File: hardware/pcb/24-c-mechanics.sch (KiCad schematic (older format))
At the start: 24 parts, among them U301 VID28-05, U302 VID66-08, U303 AH3572, U304 AH3572, U305 AH3572, U306 AH3572

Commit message: First placement
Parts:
- removed TP301: MA1, TestPoint:TestPoint_Pad_D2.0mm, symbol Connector:TestPoint
- removed TP302: MA2, TestPoint:TestPoint_Pad_D2.0mm, symbol Connector:TestPoint
- removed TP304: MA3, TestPoint:TestPoint_Pad_D2.0mm, symbol Connector:TestPoint
- removed TP307: MA4, TestPoint:TestPoint_Pad_D2.0mm, symbol Connector:TestPoint
- removed TP310: MB1, TestPoint:TestPoint_Pad_D2.0mm, symbol Connector:TestPoint
- removed TP311: MB2, TestPoint:TestPoint_Pad_D2.0mm, symbol Connector:TestPoint
- removed TP312: MB3, TestPoint:TestPoint_Pad_D2.0mm, symbol Connector:TestPoint
- removed TP313: MB4, TestPoint:TestPoint_Pad_D2.0mm, symbol Connector:TestPoint
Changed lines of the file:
@@
 	6750 4300 7500 4300
-$Comp
-L Connector:TestPoint TP301
-U 1 1 5FF9F67F
-P 9350 1500
-F 0 "TP301" V 9350 1700 50  0000 L CNN
-F 1 "MA1" H 9408 1527 50  0001 L CNN
-F 2 "TestPoint:TestPoint_Pad_D2.0mm" H 9550 1500 50  0001 C CNN
-F 3 "~" H 9550 1500 50  0001 C CNN
-	1    9350 1500
-	0    1    -1   0
-$EndComp
-$Comp
-L Connector:TestPoint TP302
-U 1 1 5FFA0591
-P 9350 1600
-F 0 "TP302" V 9350 1800 50  0000 L CNN
-F 1 "MA2" H 9408 1627 50  0001 L CNN
-F 2 "TestPoint:TestPoint_Pad_D2.0mm" H 9550 1600 50  0001 C CNN
-F 3 "~" H 9550 1600 50  0001 C CNN
-	1    9350 1600
-	0    1    -1   0
-$EndComp
-$Comp
-L Connector:TestPoint TP304
-U 1 1 5FFA0852
-P 9350 1700
-F 0 "TP304" V 9350 1900 50  0000 L CNN
-F 1 "MA3" H 9408 1727 50  0001 L CNN
-F 2 "TestPoint:TestPoint_Pad_D2.0mm" H 9550 1700 50  0001 C CNN
-F 3 "~" H 9550 1700 50  0001 C CNN
-	1    9350 1700
-	0    1    -1   0
-$EndComp
-$Comp
-L Connector:TestPoint TP307
-U 1 1 5FFA0AC7
-P 9350 1800
-F 0 "TP307" V 9350 2000 50  0000 L CNN
-F 1 "MA4" H 9408 1827 50  0001 L CNN
-F 2 "TestPoint:TestPoint_Pad_D2.0mm" H 9550 1800 50  0001 C CNN
-F 3 "~" H 9550 1800 50  0001 C CNN
-	1    9350 1800
-	0    1    -1   0
-$EndComp
-Wire Wire Line
-	9350 1500 8950 1500
-Wire Wire Line
-	9350 1600 8950 1600
-Wire Wire Line
-	9350 1700 8950 1700
-Wire Wire Line
-	9350 1800 8950 1800
-$Comp
-L Connector:TestPoint TP310
-U 1 1 5FFAB35D
-P 9350 2250
-F 0 "TP310" V 9350 2450 50  0000 L CNN
-F 1 "MB1" H 9408 2277 50  0001 L CNN
-F 2 "TestPoint:TestPoint_Pad_D2.0mm" H 9550 2250 50  0001 C CNN
-F 3 "~" H 9550 2250 50  0001 C CNN
-	1    9350 2250
-	0    1    -1   0
-$EndComp
-$Comp
-L Connector:TestPoint TP311
-U 1 1 5FFAB363
-P 9350 2350
-F 0 "TP311" V 9350 2550 50  0000 L CNN
-F 1 "MB2" H 9408 2377 50  0001 L CNN
-F 2 "TestPoint:TestPoint_Pad_D2.0mm" H 9550 2350 50  0001 C CNN
-F 3 "~" H 9550 2350 50  0001 C CNN
-	1    9350 2350
-	0    1    -1   0
-$EndComp
-$Comp
-L Connector:TestPoint TP312
-U 1 1 5FFAB369
-P 9350 2450
-F 0 "TP312" V 9350 2650 50  0000 L CNN
-F 1 "MB3" H 9408 2477 50  0001 L CNN
-F 2 "TestPoint:TestPoint_Pad_D2.0mm" H 9550 2450 50  0001 C CNN
-F 3 "~" H 9550 2450 50  0001 C CNN
-	1    9350 2450
-	0    1    -1   0
-$EndComp
-$Comp
-L Connector:TestPoint TP313
-U 1 1 5FFAB36F
-P 9350 2550
-F 0 "TP313" V 9350 2750 50  0000 L CNN
-F 1 "MB4" H 9408 2577 50  0001 L CNN
-F 2 "TestPoint:TestPoint_Pad_D2.0mm" H 9550 2550 50  0001 C CNN
-F 3 "~" H 9550 2550 50  0001 C CNN
-	1    9350 2550
-	0    1    -1   0
-$EndComp
-Wire Wire Line
-	9350 2250 8950 2250
-Wire Wire Line
-	9350 2350 8950 2350
-Wire Wire Line
-	9350 2450 8950 2450
-Wire Wire Line
-	9350 2550 8950 2550
-Text Label 8950 1500 0    50   ~ 0
-MA1
-Text Label 8950 1600 0    50   ~ 0
-MA2
-Text Label 8950 1700 0    50   ~ 0
-MA3
-Text Label 8950 1800 0    50   ~ 0
-MA4
-Text Label 8950 2250 0    50   ~ 0
-MB1
-Text Label 8950 2350 0    50   ~ 0
-MB2
-Text Label 8950 2450 0    50   ~ 0
-MB3
-Text Label 8950 2550 0    50   ~ 0
-MB4
 $Comp
 L Connector:TestPoint TP309

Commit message: Finished routing
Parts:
- U301: footprint mvl-footprints:vid_28_05 -> mvl-footprints:BK30D-R5
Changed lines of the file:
@@
 F 0 "U301" H 8050 1865 50  0000 C CNN
 F 1 "VID28-05" H 8050 1774 50  0000 C CNN
-F 2 "mvl-footprints:vid_28_05" H 8050 1150 50  0001 C CNN
+F 2 "mvl-footprints:BK30D-R5" H 8050 1150 50  0001 C CNN
 F 3 "http://www.vidmotion.com.cn/UploadFile/pdf/product/20090905105654VID28-05%20V2070829.pdf" H 7700 1500 50  0001 C CNN
 F 4 "-MASTER" H 8050 1500 50  0001 C CNN "Config"
@@
 F 0 "U301" H 8050 2615 50  0000 C CNN
 F 1 "VID28-05" H 8050 2524 50  0000 C CNN
-F 2 "mvl-footprints:vid_28_05" H 8050 1900 50  0001 C CNN
+F 2 "mvl-footprints:BK30D-R5" H 8050 1900 50  0001 C CNN
 F 3 "http://www.vidmotion.com.cn/UploadFile/pdf/product/20090905105654VID28-05%20V2070829.pdf" H 7700 2250 50  0001 C CNN
 F 4 "-MASTER" H 8050 2250 50  0001 C CNN "Config"

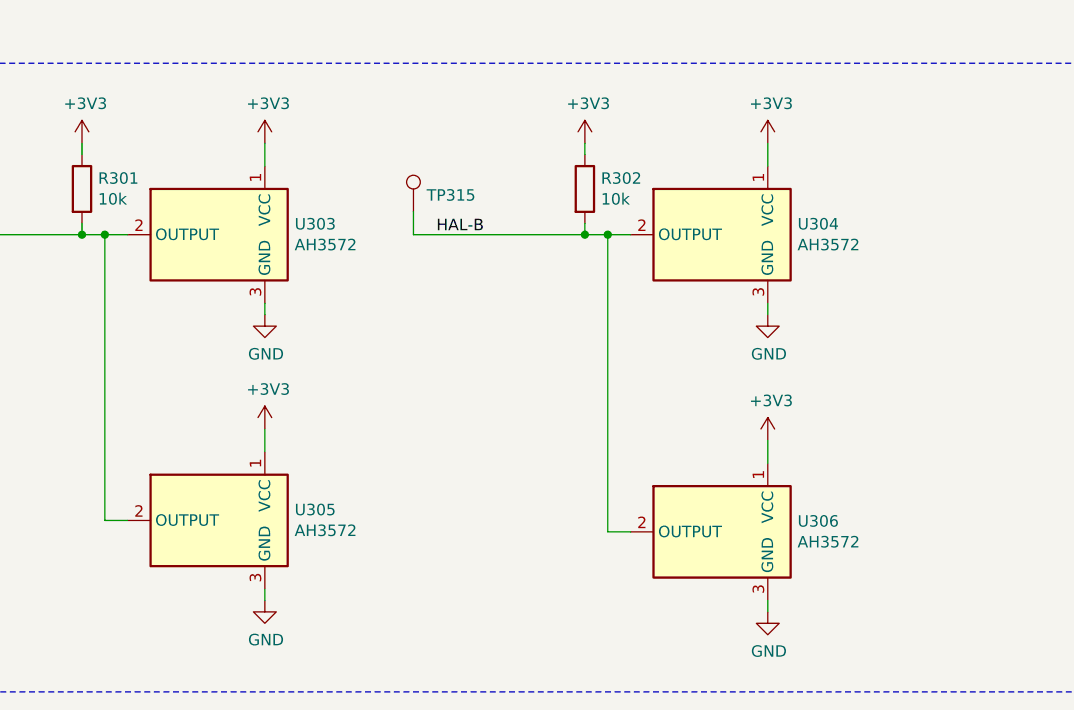
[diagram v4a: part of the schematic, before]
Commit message: Added caps to hall sensors
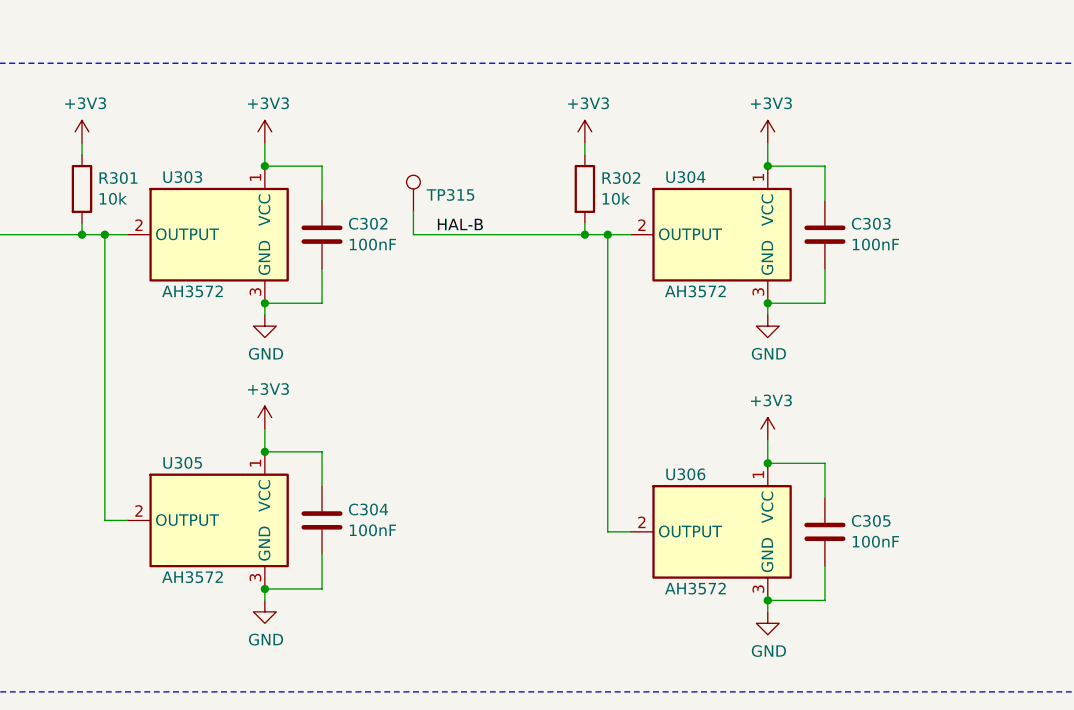
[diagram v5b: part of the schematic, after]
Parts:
- added C302, C303, C304, C305: 100nF, Capacitor_SMD:C_0603_1608Metric, symbol Device:C
- U303, U304: Config -MASTER -> -MASTER,-SLAVE
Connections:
- net +3V3: now also C302.2, C303.2, C304.2, C305.2
- net GND: now also C302.1, C303.1, C304.1, C305.1
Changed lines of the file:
@@
 AR Path="/5FCEC14D" Ref="U?"  Part="1"
 AR Path="/5FCDA719/5FCEC14D" Ref="U303"  Part="1"
-F 0 "U303" H 5570 4346 50  0000 R CNN
-F 1 "AH3572" H 5570 4255 50  0000 R CNN
+F 0 "U303" H 6150 4550 50  0000 R CNN
+F 1 "AH3572" H 6150 4050 50  0000 R CNN
 F 2 "mvl-footprints:SOT-23-UD" H 5850 4300 50  0001 C CNN
 F 3 "https://www.diodes.com/assets/Datasheets/AH3572.pdf" H 5850 4300 50  0001 C CNN
-F 4 "-MASTER" H 5900 4300 50  0001 C CNN "Config"
+F 4 "-MASTER,-SLAVE" H 5900 4300 50  0001 C CNN "Config"
 	1    5900 4300
 	-1   0    0    -1
@@
 	5300 4300 5300 4250
 Wire Wire Line
-	6100 3900 6100 4000
-Wire Wire Line
 	5300 3900 5300 3950
 Wire Wire Line
@@
 AR Path="/5FCEC173" Ref="U?"  Part="1"
 AR Path="/5FCDA719/5FCEC173" Ref="U304"  Part="1"
-F 0 "U304" H 7770 4346 50  0000 R CNN
-F 1 "AH3572" H 7770 4255 50  0000 R CNN
+F 0 "U304" H 8350 4550 50  0000 R CNN
+F 1 "AH3572" H 8350 4050 50  0000 R CNN
 F 2 "mvl-footprints:SOT-23-UD" H 8050 4300 50  0001 C CNN
 F 3 "https://www.diodes.com/assets/Datasheets/AH3572.pdf" H 8050 4300 50  0001 C CNN
-F 4 "-MASTER" H 8100 4300 50  0001 C CNN "Config"
+F 4 "-MASTER,-SLAVE" H 8100 4300 50  0001 C CNN "Config"
 	1    8100 4300
 	-1   0    0    -1
@@
 AR Path="/5FF39145" Ref="U?"  Part="1"
 AR Path="/5FCDA719/5FF39145" Ref="U305"  Part="1"
-F 0 "U305" H 5570 5596 50  0000 R CNN
-F 1 "AH3572" H 5570 5505 50  0000 R CNN
+F 0 "U305" H 6150 5800 50  0000 R CNN
+F 1 "AH3572" H 6150 5300 50  0000 R CNN
 F 2 "Package_TO_SOT_SMD:TSOT-23" H 5850 5550 50  0001 C CNN
 F 3 "https://www.diodes.com/assets/Datasheets/AH3572.pdf" H 5850 5550 50  0001 C CNN
@@
 AR Path="/5FF3B4AC" Ref="U?"  Part="1"
 AR Path="/5FCDA719/5FF3B4AC" Ref="U306"  Part="1"
-F 0 "U306" H 7770 5646 50  0000 R CNN
-F 1 "AH3572" H 7770 5555 50  0000 R CNN
+F 0 "U306" H 8350 5850 50  0000 R CNN
+F 1 "AH3572" H 8350 5350 50  0000 R CNN
 F 2 "Package_TO_SOT_SMD:TSOT-23" H 8050 5600 50  0001 C CNN
 F 3 "https://www.diodes.com/assets/Datasheets/AH3572.pdf" H 8050 5600 50  0001 C CNN
@@
 Wire Notes Line
 	10050 3550 10050 6300
+$Comp
+L Device:C C?
+U 1 1 6027E633
+P 8550 4300
+AR Path="/6027E633" Ref="C?"  Part="1"
+AR Path="/5FCDA719/6027E633" Ref="C303"  Part="1"
+F 0 "C303" H 8436 4254 50  0000 R CNN
+F 1 "100nF" H 8436 4345 50  0000 R CNN
+F 2 "Capacitor_SMD:C_0603_1608Metric" H 8588 4150 50  0001 C CNN
+F 3 "~" H 8550 4300 50  0001 C CNN
+F 4 "-MASTER,-SLAVE" H 8550 4300 50  0001 C CNN "Config"
+	1    8550 4300
+	-1   0    0    1
+$EndComp
+Wire Wire Line
+	8550 4150 8550 4000
+Wire Wire Line
+	8550 4450 8550 4600
+Wire Wire Line
+	8550 4600 8300 4600
+Wire Wire Line
+	6100 3900 6100 4000
+Wire Wire Line
+	8550 4000 8300 4000
+Connection ~ 8300 4000
+Connection ~ 8300 4600
+$Comp
+L Device:C C?
+U 1 1 60289646
+P 8550 5600
+AR Path="/60289646" Ref="C?"  Part="1"
+AR Path="/5FCDA719/60289646" Ref="C305"  Part="1"
+F 0 "C305" H 8436 5554 50  0000 R CNN
+F 1 "100nF" H 8436 5645 50  0000 R CNN
+F 2 "Capacitor_SMD:C_0603_1608Metric" H 8588 5450 50  0001 C CNN
+F 3 "~" H 8550 5600 50  0001 C CNN
+F 4 "-MASTER" H 8550 5600 50  0001 C CNN "Config"
+	1    8550 5600
+	-1   0    0    1
+$EndComp
+Wire Wire Line
+	8550 5450 8550 5300
+Wire Wire Line
+	8550 5750 8550 5900
+$Comp
+L Device:C C?
+U 1 1 6028B894
+P 6350 4300
+AR Path="/6028B894" Ref="C?"  Part="1"
+AR Path="/5FCDA719/6028B894" Ref="C302"  Part="1"
+F 0 "C302" H 6236 4254 50  0000 R CNN
+F 1 "100nF" H 6236 4345 50  0000 R CNN
+F 2 "Capacitor_SMD:C_0603_1608Metric" H 6388 4150 50  0001 C CNN
+F 3 "~" H 6350 4300 50  0001 C CNN
+F 4 "-MASTER,-SLAVE" H 6350 4300 50  0001 C CNN "Config"
+	1    6350 4300
+	-1   0    0    1
+$EndComp
+Wire Wire Line
+	6350 4150 6350 4000
+Wire Wire Line
+	6350 4450 6350 4600
+$Comp
+L Device:C C?
+U 1 1 6028DAB7
+P 6350 5550
+AR Path="/6028DAB7" Ref="C?"  Part="1"
+AR Path="/5FCDA719/6028DAB7" Ref="C304"  Part="1"
+F 0 "C304" H 6236 5504 50  0000 R CNN
+F 1 "100nF" H 6236 5595 50  0000 R CNN
+F 2 "Capacitor_SMD:C_0603_1608Metric" H 6388 5400 50  0001 C CNN
+F 3 "~" H 6350 5550 50  0001 C CNN
+F 4 "-MASTER" H 6350 5550 50  0001 C CNN "Config"
+	1    6350 5550
+	-1   0    0    1
+$EndComp
+Wire Wire Line
+	6350 5400 6350 5250
+Wire Wire Line
+	6350 5700 6350 5850
+Wire Wire Line
+	8550 5300 8300 5300
+Connection ~ 8300 5300
+Wire Wire Line
+	8550 5900 8300 5900
+Connection ~ 8300 5900
+Wire Wire Line
+	6350 5850 6100 5850
+Connection ~ 6100 5850
+Wire Wire Line
+	6350 5250 6100 5250
+Connection ~ 6100 5250
+Wire Wire Line
+	6350 4600 6100 4600
+Connection ~ 6100 4600
+Wire Wire Line
+	6350 4000 6100 4000
+Connection ~ 6100 4000
 $EndSCHEMATC
